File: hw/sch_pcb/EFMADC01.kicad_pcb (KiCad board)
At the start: 4 copper layers, 80 x 80 mm, 89 parts, among them J1 SM06B-GHS-TB, J2 SM03B-GHS-TB, J3 HEADER_1x01, J4 HEADER_2x03, J5 SM08B-GHS-TB, J6 SM06B-GHS-TB, SW1 KMT031 NGJ LHS C&K, U1 ISL21080DIH312Z-TK 1V25, U10 SN74LVC1G14QDCKRQ1, U11 SN74LVC1G14QDCKRQ1, U12 SN74LVC1G14QDCKRQ1, U13 VCNT2020, U2 OPA314, U3 MIC5504-3.3YM5, U4 PCF8583, U5 VCNT2020, U6 VCNT2020, U7 SHT31, U8 ATMEGA1284P-AU, U9 AT24CS64-SSHM, Y1 16MHz

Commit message: Starting layout work.
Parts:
- removed C13, C14, C16, C18, C19, C20, C22, C23, C24, C26: 100nF, Capacitor_SMD:C_0603_1608Metric
- removed C15, C17: 15 pF, Capacitor_SMD:C_0603_1608Metric
- removed C21: 10uF, Capacitor_SMD:C_0805_2012Metric
- removed C25: 4u7, Capacitor_SMD:C_0603_1608Metric
- removed D3: YELLOW, LED_SMD:LED_0603_1608Metric
- removed D4: BLUE, LED_SMD:LED_0603_1608Metric
- removed D5: GREEN, LED_SMD:LED_0603_1608Metric
- removed D6: RED, LED_SMD:LED_0603_1608Metric
- removed F1: 350mA, Fuse:Fuse_1812_4532Metric
- removed G1, G2: , MLAB_LOGA:UST
- removed J3: HEADER_1x01, Mlab_Pin_Headers:Straight_1x01
- removed JP2, JP3: SolderJumper_2_Open, Jumper:SolderJumper-2_P1.3mm_Open_RoundedPad1.0x1.5mm
- removed JP4: Jumper_2_Bridged, NetTie:NetTie-2_SMD_Pad0.5mm
- removed JP5: SolderJumper_2_Bridged, Jumper:SolderJumper-2_P1.3mm_Bridged_RoundedPad1.0x1.5mm
- removed L1: 10uH - LQH32CN100K23L, Inductor_SMD:L_1210_3225Metric
- removed R10, R11, R28: 4k7, Resistor_SMD:R_0603_1608Metric
- removed R12, R13, R14, R6, R7: 10k, Resistor_SMD:R_0603_1608Metric
- removed R15, R18, R21, R5: 2k2, Resistor_SMD:R_0603_1608Metric
- removed R16, R17, R22, R23, R24, R25, R26: 33R, Resistor_SMD:R_0603_1608Metric
- removed R19, R20, R27, R8, R9: 100R, Resistor_SMD:R_0603_1608Metric
- removed SW1: KMT031 NGJ LHS C&K, Mlab_SW:KMT031 NGJ LHS C&K
- removed U10, U11, U12: SN74LVC1G14QDCKRQ1, Package_TO_SOT_SMD:SOT-353_SC-70-5
- removed U13, U5, U6: VCNT2020, Mlab_IO:XDCR_VCNT2020
- removed U7: SHT31, Mlab_IO:DFN-8-1EP_2.4x2.4mm_Pitch0.5mm
- removed U8: ATMEGA1284P-AU, Package_QFP:TQFP-44_10x10mm_P0.8mm
- removed U9: AT24CS64-SSHM, Package_SO:SOIC-8_3.9x4.9mm_P1.27mm
- removed Y1: 16MHz, Mlab_XTAL:Crystal SMD CFPX-180
- added FID1: Fiducial, Fiducial:Fiducial_1mm_Mask2mm, B.Cu at (167.8, 87.7)
- added FID2: Fiducial, Fiducial:Fiducial_1mm_Mask2mm, B.Cu at (120.8, 113.6)
- added J7: HEADER_2x01_PARALLEL, Mlab_Pin_Headers:Straight_2x01, F.Cu at (171.6, 103.5)
- added J9: MCX, Connector_Coaxial:SMA_Amphenol_901-144_Vertical, F.Cu at (124.1, 105.0)
- added M1: RFShield_TwoPieces, RF_Shielding:Laird_Technologies_BMI-S-204-F_32.00x32.00mm, B.Cu at (148.5, 105.0)
- added M2: HOLE, Mlab_Mechanical:MountingHole_3mm, F.Cu at (123.1, 89.8)
- added M3: HOLE, Mlab_Mechanical:MountingHole_3mm, F.Cu at (173.9, 89.8)
- added M4: HOLE, Mlab_Mechanical:MountingHole_3mm, F.Cu at (123.1, 120.2)
- added M5: HOLE, Mlab_Mechanical:MountingHole_3mm, F.Cu at (173.9, 120.2)
- C1, C2, C3, C4, C5, D1, R1, R2, R3, U1, U2: moved to B.Cu
- C10, C11, C12: footprint Capacitor_SMD:C_0603_1608Metric -> Capacitor_SMD:C_0805_2012Metric; moved to B.Cu
- C6: value 10uF -> 1uF; footprint Capacitor_SMD:C_0805_2012Metric -> Mlab_L:FIR_0805; moved to B.Cu
- C7: value 1uF -> 100nF; footprint Capacitor_SMD:C_0603_1608Metric -> Capacitor_SMD:C_0805_2012Metric; moved to B.Cu
- C8: value 1uF -> 10uF; footprint Capacitor_SMD:C_0603_1608Metric -> Capacitor_SMD:C_0805_2012Metric; moved to B.Cu
- C9: footprint Capacitor_SMD:C_0805_2012Metric -> Capacitor_Tantalum_SMD:CP_EIA-3216-18_Kemet-A; moved to B.Cu
- D2: value ZENER-6.2V -> BZV55C-6,2V; footprint Mlab_D:Diode-MiniMELF_Standard -> Diode_SMD:D_MiniMELF; moved to B.Cu
- J1: value SM06B-GHS-TB -> 3.3-5V; footprint Connector_JST:JST_GH_SM06B-GHS-TB_1x06-1MP_P1.25mm_Horizontal -> Mlab_Pin_Headers:Straight_2x03
- J2: value SM03B-GHS-TB -> HEADER_2x01; footprint Connector_JST:JST_GH_SM03B-GHS-TB_1x03-1MP_P1.25mm_Horizontal -> Mlab_Pin_Headers:Straight_2x01
- J4: value HEADER_2x03 -> HEADER_2x01_PARALLEL; footprint Mlab_Pin_Headers:SMD_2x03 -> Mlab_Pin_Headers:Straight_2x01; moved to F.Cu
- J5: value SM08B-GHS-TB -> HEADER_2x01_PARALLEL; footprint Connector_JST:JST_GH_SM08B-GHS-TB_1x08-1MP_P1.25mm_Horizontal -> Mlab_Pin_Headers:Straight_2x01
- J6: value SM06B-GHS-TB -> HEADER_2x01_PARALLEL; footprint Connector_JST:JST_GH_SM06B-GHS-TB_1x06-1MP_P1.25mm_Horizontal -> Mlab_Pin_Headers:Straight_2x01
- JP1: value SolderJumper_2_Bridged -> Jumper_2_Bridged; footprint Jumper:SolderJumper-2_P1.3mm_Bridged_RoundedPad1.0x1.5mm -> NetTie:NetTie-2_SMD_Pad0.5mm; moved to B.Cu
- U3: value MIC5504-3.3YM5 -> ISL21080CIH330Z-TK; footprint Package_TO_SOT_SMD:SOT-23-5 -> Package_TO_SOT_SMD:SOT-23; moved to B.Cu
- U4: value PCF8583 -> LTC1865-MS; footprint Mlab_IO:SOT176-1 -> Package_SO:MSOP-10_3x3mm_P0.5mm; moved to B.Cu
- moved J1 70.4 mm to (171.6, 110.3), turned to 0 degrees
- moved J5 65.4 mm to (171.6, 98.4), turned to 180 degrees
- moved J6 62.9 mm to (171.6, 95.9), turned to 180 degrees
- moved D2 51.7 mm to (175.9, 108.8), turned to 90 degrees
- moved C2 51.5 mm to (127.7, 105.0), turned to 0 degrees
- moved JP1 44.1 mm to (174.4, 117.6)
- moved D1 43.7 mm to (135.0, 107.0)
- moved U4 42.9 mm to (158.9, 106.0)
- moved R1 40.8 mm to (135.0, 104.0), turned to -90 degrees
- moved C6 37.7 mm to (160.7, 110.8), turned to 0 degrees
- moved C5 36.0 mm to (145.1, 107.4)
- moved R3 35.2 mm to (145.1, 114.9), turned to 180 degrees
- moved C7 30.5 mm to (150.2, 105.4), turned to 180 degrees
- moved U2 30.1 mm to (156.7, 115.6), turned to 180 degrees
- moved C8 29.7 mm to (150.2, 108.4), turned to 180 degrees
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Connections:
- C1 pad 1: PA1 -> /REF_1V25
- C10 pad 1: +3.3VA -> VCC
- C10 pad 2: GNDA -> GND
- C11 pad 1: +3V3 -> Net-(U4-V_{REF})
- C11 pad 2: GND -> GNDA
- C12 pad 1: +3V3 -> VCC
- C12 pad 2: GND -> GNDA
- C3 pad 2: PA1 -> /REF_1V25
- C4 pad 2: PA0 -> Net-(U4-CH0)
- C6 pad 1: Net-(D2-K) -> VCC
- C8 pad 1: +3V3 -> Net-(D2-K)
- C9 pad 1: +3.3VA -> VCC
- C9 pad 2: GNDA -> GND
- J1 pad 1: +5V -> GND
- J1 pad 2: Net-(J1-Pad2) -> GND
- J1 pad 3: Net-(J1-Pad3) -> Net-(D2-K)
- J1 pad 4: SCL_RPM -> Net-(D2-K)
- J1 pad 5: SDA_RPM -> GND
- J2 pad 1: PA1 -> Net-(U4-V_{REF})
- J2 pad 2: PA0 -> Net-(U3-Vout)
- J4 pad 1: /CPU/PB6 -> Net-(U4-SCK)
- J4 pad 2: +3V3 -> Net-(U4-SCK)
- J5 pad 1: /CPU/TIMEPULSE -> Net-(U4-SDO)
- J5 pad 2: /CPU/EXTINT -> Net-(U4-SDO)
- J6 pad 1: +5V -> Net-(U4-SDI)
- J6 pad 2: Net-(J6-Pad2) -> Net-(U4-SDI)
- JP1 pad 1: Net-(JP1-A) -> GNDA
- JP1 pad 2: Net-(JP1-B) -> GND
- R1 pad 1: PA1 -> /REF_1V25
- R2 pad 1: PA1 -> /REF_1V25
- R3 pad 2: PA0 -> Net-(U4-CH0)
- U1 pad 2: PA1 -> /REF_1V25
- U2 pad 1: PA0 -> Net-(U4-CH0)
- U3 pad 1: Net-(D2-K) -> VCC
- U3 pad 2: GND -> Net-(U3-Vout)
- U3 pad 3: Net-(D2-K) -> GNDA
- U4 pad 1: COUNT_1 -> Net-(U4-CONV)
- U4 pad 2: unconnected-(U4-OSCO-Pad2) -> Net-(U4-CH0)
- U4 pad 3: GND -> /REF_1V25
- U4 pad 4: GND -> GNDA
- U4 pad 5: SDA_RPM -> GND
- U4 pad 6: SCL_RPM -> Net-(U4-SDI)
- U4 pad 7: unconnected-(U4-#INT-Pad7) -> Net-(U4-SDO)
- U4 pad 8: +3V3 -> Net-(U4-SCK)
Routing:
- net +3V3: track 174.5 -> 0.00 mm, vias 5 -> 0
- net /CPU/PC0: track 88.6 -> 0.00 mm, vias 6 -> 0
- net /CPU/PC1: track 86.1 -> 0.00 mm, vias 5 -> 0
- net /CPU/TX1: track 61.4 -> 0.00 mm, vias 2 -> 0
- net +5V: track 56.5 -> 0.00 mm, vias 3 -> 0
- net /CPU/TIMEPULSE: track 55.7 -> 0.00 mm, vias 2 -> 0
- net /CPU/RX1: track 55.5 -> 0.00 mm, vias 2 -> 0
- net /CPU/RX0: track 53.7 -> 0.00 mm, vias 2 -> 0
- net /CPU/TX0: track 53.5 -> 0.00 mm, vias 2 -> 0
- net /CPU/GEO_STAT: track 51.8 -> 0.00 mm, vias 2 -> 0
- net /CPU/EXTINT: track 49.0 -> 0.00 mm
- net +3.3VA: track 44.7 -> 0.00 mm, vias 6 -> 0
- net COUNT_2: track 41.6 -> 0.00 mm, vias 2 -> 0
- net COUNT_1: track 39.9 -> 0.00 mm
- net COUNT_3: track 35.5 -> 0.00 mm, vias 4 -> 0
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- removed copper zone on B.Cu, net GND
- removed copper zone on F.Cu, net GND
- removed copper zone on In1.Cu, net GND
- removed copper zone on In2.Cu, net GND
- removed copper zone on F.Cu, net GNDA
- removed copper zone on In1.Cu, net GNDA
- removed copper zone on B.Cu, net STATOR
- removed copper zone on In1.Cu, net STATOR
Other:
- board size 80 x 80 mm -> 60.5 x 40.1 mm
- board text removed: "#RST PB7 PB6 GND PB5 3V3"
- board text removed: "Button"
- board text removed: "Connectors: J1 - Pixhawk UART & I2C J5 - Payload connector J6 - Debug & programming J2 - Measuring signal"
- board text removed: "Debug UART"
- board text removed: "LED1"
- board text removed: "LED2"
- board text removed: "LED3"
- board text removed: "ON"
- board text removed: "Payload"
- board text removed: "Pixhawk I2C & UART"
- board text removed: "USTTHUNDERMILLPCB01B 2023"

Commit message: Rounted PCB Added silkscreen text.
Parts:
- added R4: 33R, Resistor_SMD:R_0805_2012Metric, B.Cu at (167.6, 100.9)
- added R5: 33R, Resistor_SMD:R_0805_2012Metric, B.Cu at (167.6, 98.5)
- added R6: 33R, Resistor_SMD:R_0805_2012Metric, B.Cu at (167.6, 95.9)
- added R7: 33R, Resistor_SMD:R_0805_2012Metric, B.Cu at (167.4, 105.5)
- C1, C2, C3, C4, C5: footprint Capacitor_SMD:C_0603_1608Metric -> Capacitor_SMD:C_0805_2012Metric
- C6: value 1uF -> 100nF; footprint Mlab_L:FIR_0805 -> Capacitor_SMD:C_0805_2012Metric
- C9: footprint Capacitor_Tantalum_SMD:CP_EIA-3216-18_Kemet-A -> Capacitor_SMD:C_0805_2012Metric
- D1: footprint Diode_SMD:D_SOD-523 -> Diode_SMD:D_SMB
- R1, R2, R3: footprint Resistor_SMD:R_0603_1608Metric -> Resistor_SMD:R_0805_2012Metric
- moved JP1 27.0 mm to (163.8, 92.8), turned to 0 degrees
- moved C12 24.8 mm to (160.7, 95.0), turned to 90 degrees
- moved U2 20.3 mm to (138.7, 106.1), turned to 0 degrees
- moved C8 18.1 mm to (167.9, 112.1), turned to -90 degrees
- moved R2 15.2 mm to (139.1, 98.4), turned to -90 degrees
- moved R3 14.7 mm to (140.0, 101.1), turned to 0 degrees
- moved C10 12.0 mm to (159.3, 103.6), turned to -90 degrees
- moved C11 10.9 mm to (155.4, 104.8)
- moved C9 9.76 mm to (161.3, 103.6), turned to -90 degrees
- moved U1 8.63 mm to (146.0, 101.2)
- moved C7 8.17 mm to (146.0, 98.4)
- moved C6 7.55 mm to (167.9, 108.7), turned to 90 degrees
- moved U3 6.48 mm to (157.9, 95.0)
- moved U4 6.21 mm to (154.2, 102.0)
- moved C1 5.97 mm to (149.4, 101.4), turned to 90 degrees
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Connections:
- C5 pad 2: +3.3VA -> VCC
- C7 pad 1: Net-(D2-K) -> VCC
- C7 pad 2: GND -> GNDA
- C8 pad 1: Net-(D2-K) -> VCC
- D2 pad 1: Net-(D2-K) -> VCC
- J1 pad 3: Net-(D2-K) -> VCC
- J1 pad 4: Net-(D2-K) -> VCC
- J4 pad 1: Net-(U4-SCK) -> Net-(J4-Pad1)
- J4 pad 2: Net-(U4-SCK) -> Net-(J4-Pad1)
- J5 pad 1: Net-(U4-SDO) -> Net-(J5-Pad1)
- J5 pad 2: Net-(U4-SDO) -> Net-(J5-Pad1)
- J6 pad 1: Net-(U4-SDI) -> Net-(J6-Pad1)
- J6 pad 2: Net-(U4-SDI) -> Net-(J6-Pad1)
- J7 pad 1: Net-(U4-CONV) -> Net-(J7-Pad1)
- J7 pad 2: Net-(U4-CONV) -> Net-(J7-Pad1)
- U1 pad 1: +3.3VA -> VCC
- U2 pad 5: +3.3VA -> VCC
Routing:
- net VCC: track 0.00 -> 81.6 mm
- net /REF_1V25: track 0.00 -> 23.8 mm
- net Net-(U4-CH0): track 0.00 -> 22.0 mm
- net Net-(U4-CONV): track 0.00 -> 19.0 mm
- net Net-(U4-SDI): track 0.00 -> 16.7 mm
- net GND: track 0.00 -> 14.4 mm, vias 0 -> 4
- net Net-(D1-A1): track 0.00 -> 13.8 mm
- net Net-(U4-SCK): track 0.00 -> 11.8 mm
- net Net-(U4-SDO): track 0.00 -> 11.5 mm
- net Net-(U4-V_{REF}): track 0.00 -> 7.79 mm
- net Net-(U2--): track 0.00 -> 6.28 mm
- net Net-(J7-Pad1): track 0.00 -> 5.40 mm
- net GNDA: track 0.00 -> 5.26 mm
- net Net-(J5-Pad1): track 0.00 -> 4.47 mm
- net Net-(J6-Pad1): track 0.00 -> 4.42 mm
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- added copper zone on B.Cu, net GND
- added copper zone on F.Cu, net GND
- added copper zone on B.Cu, net GNDA
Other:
- copper layers 4 -> 2
- rule pad_to_mask_clearance: 0.1 -> 0.05
- board text added: "ADC_REF"
- board text added: "CONV"
- board text added: "EFMADC01A"
- board text added: "GND"
- board text added: "Kaklik 2025"
- board text added: "REF_out"
- board text added: "SCK"
- board text added: "SDI"
- board text added: "SDO"
- board text added: "Vcc"

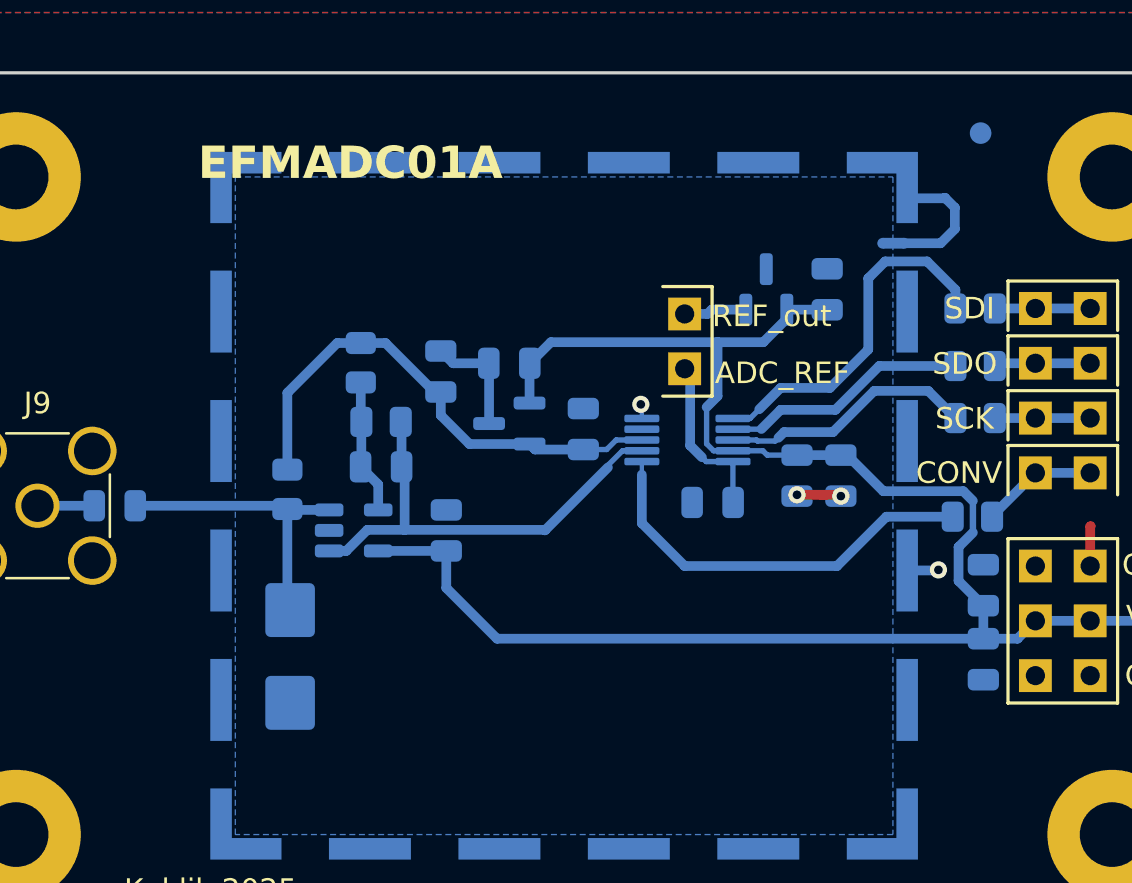
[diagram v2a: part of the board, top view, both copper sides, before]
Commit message: Improve silkscreen texts.
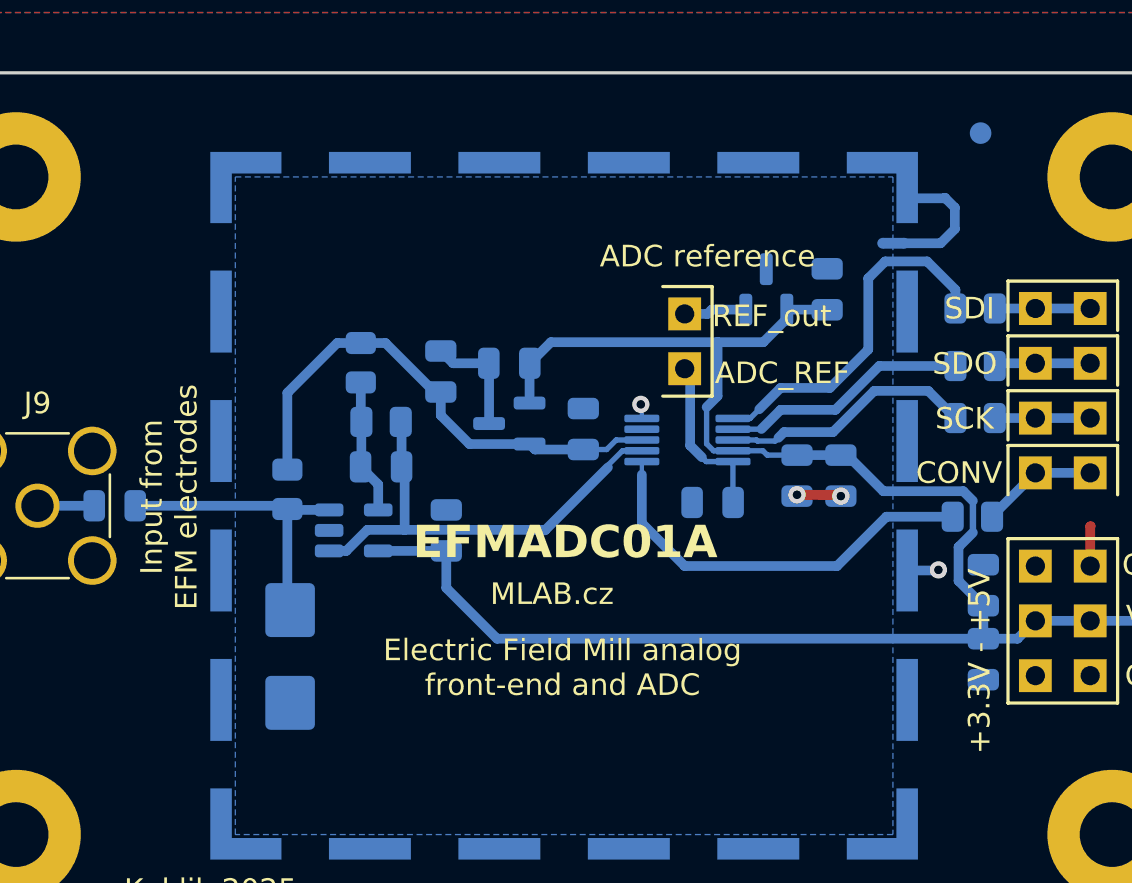
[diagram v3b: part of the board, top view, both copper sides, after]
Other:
- board text added: "+3.3V - +5V"
- board text added: "ADC reference"
- board text added: "Electric Field Mill analog front-end and ADC"
- board text added: "Input from EFM electrodes"
- board text added: "MLAB.cz"
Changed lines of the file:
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@@
 		(tags "fiducial")
 		(property "Reference" "FID2"
-			(at 0 2 0)
+			(at -0.0762 1.8288 0)
 			(layer "B.SilkS")
 			(effects
@@
 		(tags "capacitor")
 		(property "Reference" "C2"
-			(at 2.6162 -0.0762 -90)
+			(at 1.8034 -1.6256 0)
 			(layer "B.SilkS")
 			(effects
@@
 		(tags "fiducial")
 		(property "Reference" "FID1"
-			(at 0 2 0)
+			(at 2.7686 1.1176 0)
 			(layer "B.SilkS")
 			(effects
@@
 		(tags "resistor")
 		(property "Reference" "R3"
-			(at -2.667 0.1778 360)
+			(at -2.667 0.1778 0)
 			(layer "B.SilkS")
 			(effects
@@
 		)
 		(property "Value" "10k"
-			(at 0 -1.65 360)
+			(at 0 -1.65 0)
 			(layer "B.Fab")
 			(effects
@@
 		)
 		(fp_text user "${REFERENCE}"
-			(at 0 0 360)
+			(at 0 0 0)
 			(layer "B.Fab")
 			(effects
@@
 		(tags "resistor")
 		(property "Reference" "R1"
-			(at -2.7178 -0.0254 90)
+			(at 0.1524 1.4732 90)
 			(layer "B.SilkS")
 			(effects
@@
 		(tags "MSOP SO")
 		(property "Reference" "U4"
-			(at 2.5908 -2.4638 0)
+			(at -2.2352 2.8194 0)
 			(layer "B.SilkS")
 			(effects
@@
 		(tags "SOT TO_SOT_SMD")
 		(property "Reference" "U2"
-			(at 1.0668 2.5908 360)
+			(at 1.0668 2.5908 0)
 			(layer "B.SilkS")
 			(effects
@@
 		)
 		(property "Value" "OPA314"
-			(at 0 -2.4 360)
+			(at 0 -2.4 0)
 			(layer "B.Fab")
 			(effects
@@
 		)
 		(property "Footprint" "Package_TO_SOT_SMD:SOT-23-5"
-			(at 0 0 360)
+			(at 0 0 0)
 			(layer "B.Fab")
 			(hide yes)
@@
 		)
 		(property "Datasheet" "http://www.ti.com/lit/ds/symlink/opa330.pdf"
-			(at 0 0 360)
+			(at 0 0 0)
 			(layer "B.Fab")
 			(hide yes)
@@
 		)
 		(property "Description" "50μV V OS, 0.25μV/°C, 35μA CMOS OPERATIONAL AMPLIFIERS, Zerø-Drift Series, SOT"
-			(at 0 0 360)
+			(at 0 0 0)
 			(layer "B.Fab")
 			(hide yes)
@@
 		)
 		(fp_text user "${REFERENCE}"
-			(at 0 0 360)
+			(at 0 0 0)
 			(layer "B.Fab")
 			(effects
@@
 		(tags "capacitor")
 		(property "Reference" "C4"
-			(at 2.8956 -0.0254 360)
+			(at 2.8194 -0.0254 0)
 			(layer "B.SilkS")
 			(effects
@@
 		)
 		(property "Value" "1nF"
-			(at 0 -1.68 360)
+			(at 0 -1.68 0)
 			(layer "B.Fab")
 			(effects
@@
 		)
 		(fp_text user "${REFERENCE}"
-			(at 0 0 360)
+			(at 0 0 0)
 			(layer "B.Fab")
 			(effects
@@
 		(tags "net tie")
 		(property "Reference" "JP1"
-			(at 0 1.2 360)
+			(at 0 1.2 0)
 			(layer "B.SilkS")
 			(hide yes)
@@
 		)
 		(property "Value" "Jumper_2_Bridged"
-			(at 0 -1.2 360)
+			(at 0 -1.2 0)
 			(layer "B.Fab")
 			(hide yes)
@@
 	)
 	(gr_text "EFMADC01A"
-		(at 131.5328 89.9886 0)
+		(at 141.4896 107.5654 0)
 		(layer "F.SilkS")
 		(effects
@@
 		)
 	)
+	(gr_text "+3.3V - +5V"
+		(at 168.3374 116.5062 90)
+		(layer "F.SilkS")
+		(effects
+			(font
+				(size 1 1)
+				(thickness 0.15)
+			)
+			(justify left bottom)
+		)
+	)
 	(gr_text "CONV"
 		(at 164.8068 104.0602 0)
@@
 		)
 	)
+	(gr_text "Electric Field Mill analog\nfront-end and ADC "
+		(at 148.4238 113.89 0)
+		(layer "F.SilkS")
+		(effects
+			(font
+				(size 1 1)
+				(thickness 0.15)
+			)
+			(justify bottom)
+		)
+	)
 	(gr_text "Vcc"
 		(at 174.535 110.715 0)
@@
 		)
 	)
+	(gr_text "Input from \nEFM electrodes"
+		(at 131.5836 104.5936 90)
+		(layer "F.SilkS")
+		(effects
+			(font
+				(size 1 1)
+				(thickness 0.15)
+			)
+			(justify bottom)
+		)
+	)
+	(gr_text "ADC reference"
+		(at 150.151 94.0272 0)
+		(layer "F.SilkS")
+		(effects
+			(font
+				(size 1 1)
+				(thickness 0.15)
+			)
+			(justify left bottom)
+		)
+	)
 	(gr_text "Kaklik 2025"
 		(at 128.1038 123.3896 0)
@@
 		(layer "F.SilkS")
 		(effects
+			(font
+				(size 1 1)
+				(thickness 0.15)
+			)
+			(justify left bottom)
+		)
+	)
+	(gr_text "MLAB.cz"
+		(at 145.071 109.6736 0)
+		(layer "F.SilkS")
+		(effects
